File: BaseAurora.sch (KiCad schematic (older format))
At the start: 13 parts

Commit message: esquematico revisado
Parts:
- removed Cin, Cout: 1μF C, symbol Device:C
- removed D?: DIODE, symbol pspice:DIODE
- removed R? (x2): R, symbol Device:R
- removed U?: STM32F030C8Tx, Package_QFP:LQFP-48_7x7mm_P0.5mm, symbol MCU_ST_STM32F0:STM32F030C8Tx
- removed U? (x2): KA78M05_TO252, Package_TO_SOT_SMD:TO-252-2, symbol Regulator_Linear:KA78M05_TO252
- removed Vcc: Battery_Cell, Battery:BatteryHolder_Keystone_2466_1xAAA, symbol Device:Battery_Cell
- added BT?: Battery_Cell, symbol Device:Battery_Cell
- added C? (x2): 10u, symbol Device:C_Small
- added D? (x3): LED_Small, symbol Device:LED_Small
- added D?: D_Small, symbol Device:D_Small
- added F? (x2): Polyfuse_Small, symbol Device:Polyfuse_Small
- added J? (x2): Screw_Terminal_01x02, symbol Connector:Screw_Terminal_01x02
- added J? (x3): Conn_01x04_Male, symbol Connector:Conn_01x04_Male
- added J?: Conn_01x03_Male, symbol Connector:Conn_01x03_Male
- added R? (x10): R_Small, symbol Device:R_Small
- added R?: 1M, symbol Device:R_Small
- added R?: 0, symbol Device:R_Small
- added R?: 100K, symbol Device:R_Small
- added R?: 220K, symbol Device:R_Small
- added U?: E32-915T20D, symbol LoRA:E32-915T20D
- added U?: ME6217C33M5G, symbol BaseAurora:ME6217C33M5G
- added U?: NodeMCU1.0(ESP-12E), symbol MCU_ESP82:NodeMCU1.0(ESP-12E)
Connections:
- net labels added: 3V3, ADC, AcionamentoNiCd, DIO1, DIO2, GND_ISO, InputLora, LedAcionamento, LedAlimentacao, LedErro, M0Lora, M1Lora, OutputLora, SCL_MASTER, SCL_SLAVE, SDA_MASTER, SDA_SLAVE, StatusLora, VCC_ISO, VCC_MCU, VLora, Vbat, Vext
- net labels removed: VCC, Vcc
- wire segments 18 -> 32
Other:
- moved on the sheet: D?

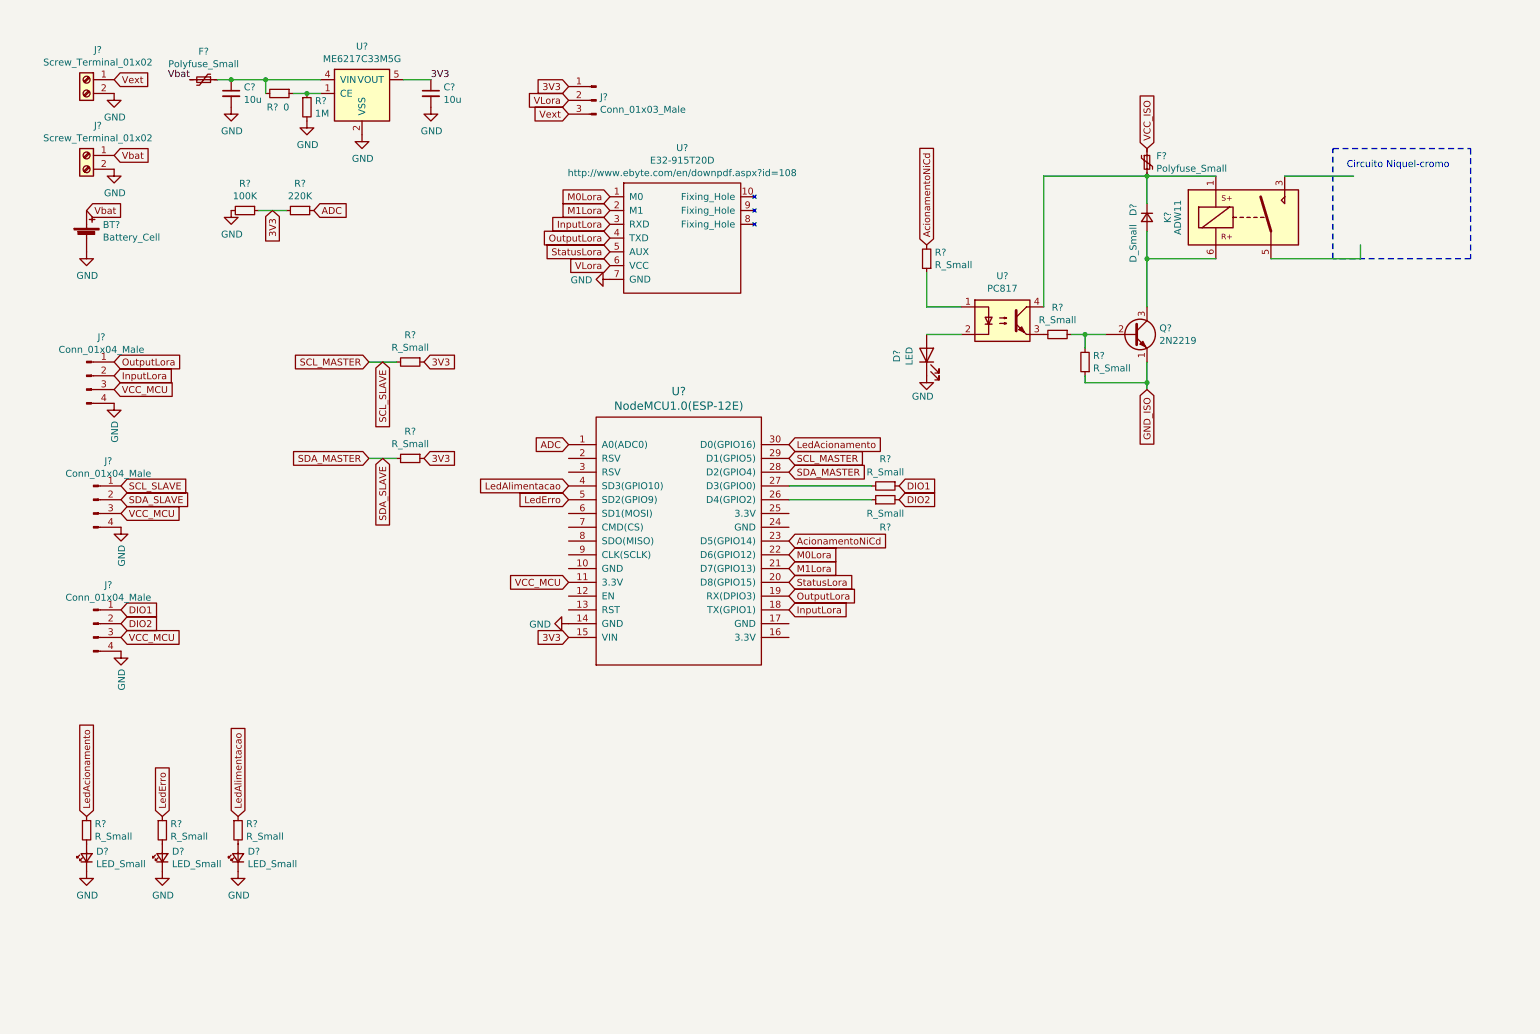
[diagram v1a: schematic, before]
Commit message: Revisão do circuito de acionamento. Atribuição de valores para os componentes. Organização geral do esquemático.
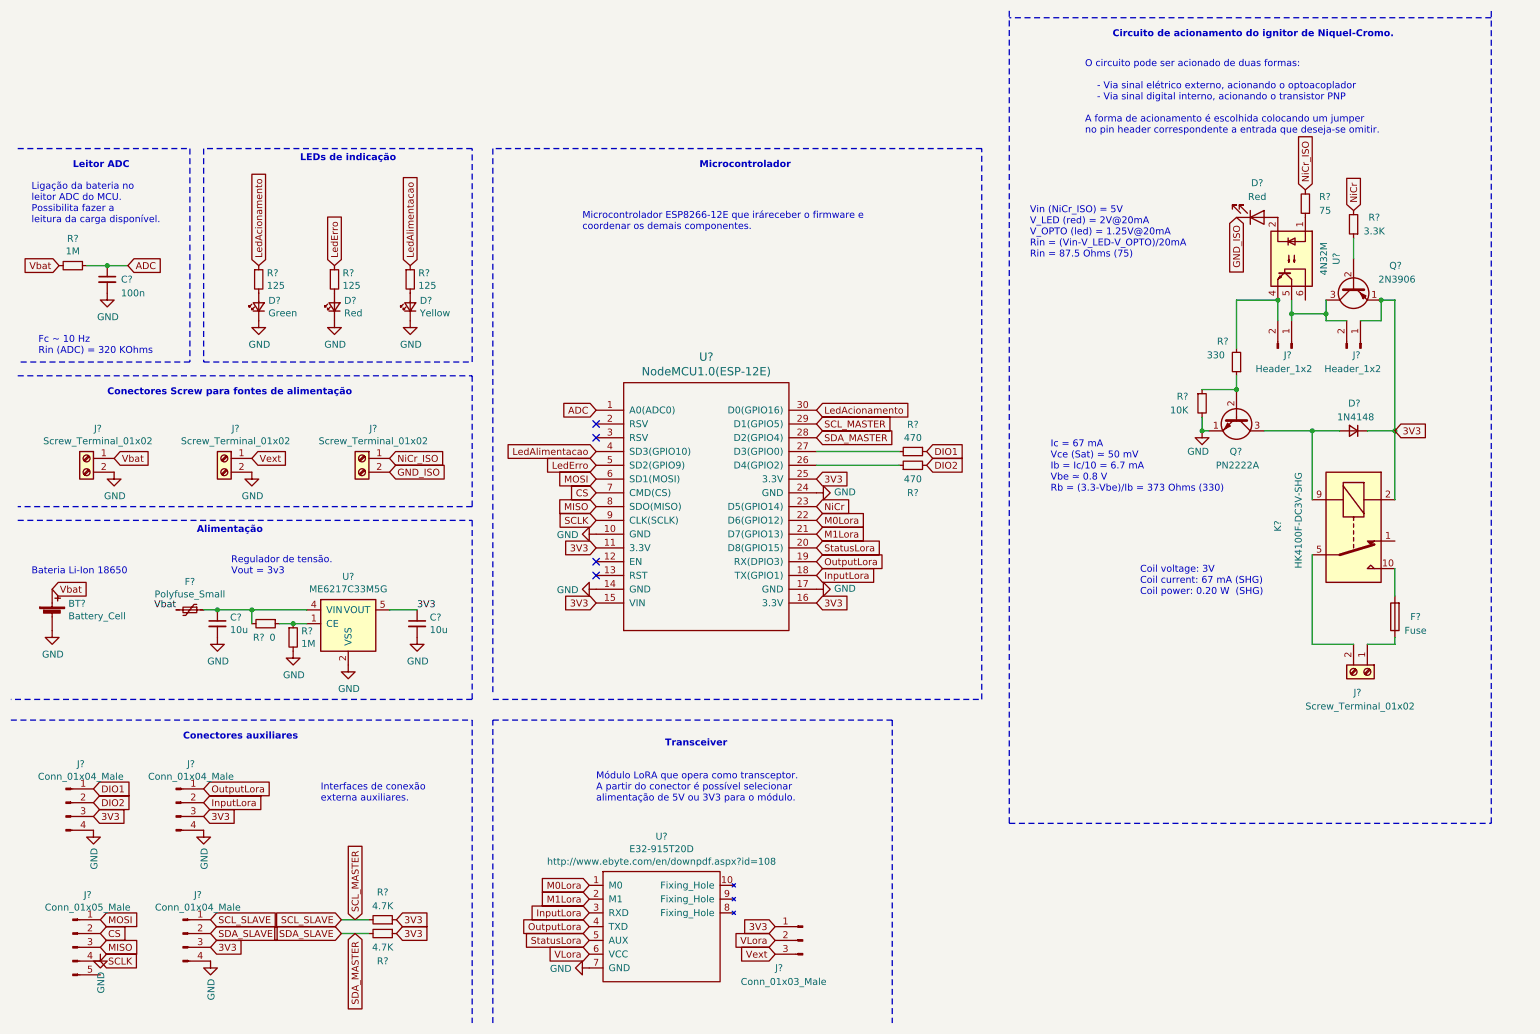
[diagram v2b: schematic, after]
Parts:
- removed F?: Polyfuse_Small, symbol Device:Polyfuse_Small
- removed K?: ADW11, Relay_THT:Relay_1P1T_NO_10x24x18.8mm_Panasonic_ADW11xxxxW_THT, symbol Relay:ADW11
- removed Q?: 2N2219, Package_TO_SOT_THT:TO-39-3, symbol Transistor_BJT:2N2219
- removed R?: 100K, symbol Device:R_Small
- removed U?: PC817, Package_DIP:DIP-4_W7.62mm, symbol Isolator:PC817
- added C?: 100n, symbol Device:C_Small
- added F?: Fuse, symbol Device:Fuse
- added J? (x2): Screw_Terminal_01x02, symbol Connector:Screw_Terminal_01x02
- added J? (x2): Header_1x2, symbol Connector:Conn_01x02_Male
- added J?: Conn_01x05_Male, symbol Connector:Conn_01x05_Male
- added K?: HK4100F-DC3V-SHG, Relay_THT:Relay_SPDT_Omron_G5V-1, symbol Relay:G5V-1
- added Q?: PN2222A, Package_TO_SOT_THT:TO-92_Inline, symbol Transistor_BJT:PN2222A
- added Q?: 2N3906, Package_TO_SOT_THT:TO-92_Inline, symbol Transistor_BJT:2N3906
- added R?: 3.3K, symbol Device:R_Small
- added U?: 4N32M, Package_DIP:DIP-6_W7.62mm, symbol Isolator:4N25
- D?: value LED -> Red
- D?: value LED_Small -> Green
- D?: value LED_Small -> Red
- D?: value LED_Small -> Yellow
- D?: value D_Small -> 1N4148
- R? (x3): value R_Small -> 125
- R? (x2): value R_Small -> 4.7K
- R? (x2): value R_Small -> 470
- R?: value R_Small -> 330
- R?: value R_Small -> 10K
- R?: value R_Small -> 75
- R?: value 220K -> 1M
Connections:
- net labels added: CS, MISO, MOSI, NiCr, NiCr_ISO, SCLK
- net labels removed: AcionamentoNiCd, VCC_ISO, VCC_MCU
- wire segments 32 -> 41
- no-connect marks 0 -> 4
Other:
- note added: "Alimentação\n"
- note added: "Bateria Li-Ion 18650"
- note added: "Circuito de acionamento do ignitor de Niquel-Cromo."
- note added: "Coil voltage: 3V\nCoil current: 67 mA (SHG)\nCoil power: 0.20 W (SHG)"
- note added: "Conectores Screw para fontes de alimentação"
- note added: "Conectores auxiliares"
- note added: "Fc ~~ 10 Hz\nRin (ADC) = 320 KOhms"
- note added: "Ic = 67 mA\nVce (Sat) ≃ 50 mV\nIb = Ic/10 = 6.7 mA\nVbe ≃ 0.8 V\nRb = (3.3-Vbe)/Ib = 373 Ohms (330)"
- note added: "Interfaces de conexão \nexterna auxiliares."
- note added: "LEDs de indicação\n"
- note added: "Leitor ADC"
- note added: "Ligação da bateria no \nleitor ADC do MCU.\nPossibilita fazer a \nleitura da carga disponível."
- note added: "Microcontrolador"
- note added: "Microcontrolador ESP8266-12E que iráreceber o firmware e \ncoordenar os demais componentes."
- note added: "Módulo LoRA que opera como transceptor.\nA partir do conector é possível selecionar\nalimentação de 5V ou 3V3 para o módulo."
- note added: "O circuito pode ser acionado de duas formas:\n\n - Via sinal elétrico externo, acionando o optoacoplador\n - Via sinal digital interno, acionando o transistor PNP\n\nA forma de acionamento é escolhida colocando um jumper \nno pin header correspondente a entrada que deseja-se omitir."
- note added: "Regulador de tensão.\nVout = 3v3\n"
- note added: "Transceiver"
- note added: "Vin (NiCr_ISO) = 5V\nV_LED (red) = 2V@20mA\nV_OPTO (led) = 1.25V@20mA\nRin = (Vin-V_LED-V_OPTO)/20mA \nRin = 87.5 Ohms (75)"
- note removed: "Circuito Niquel-cromo"
- moved on the sheet: BT?, C?, D?, F?, J?, R?, U?

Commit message: Reorganização dos componentes e posicionamento do acionamento do NiCr no pino seguro.
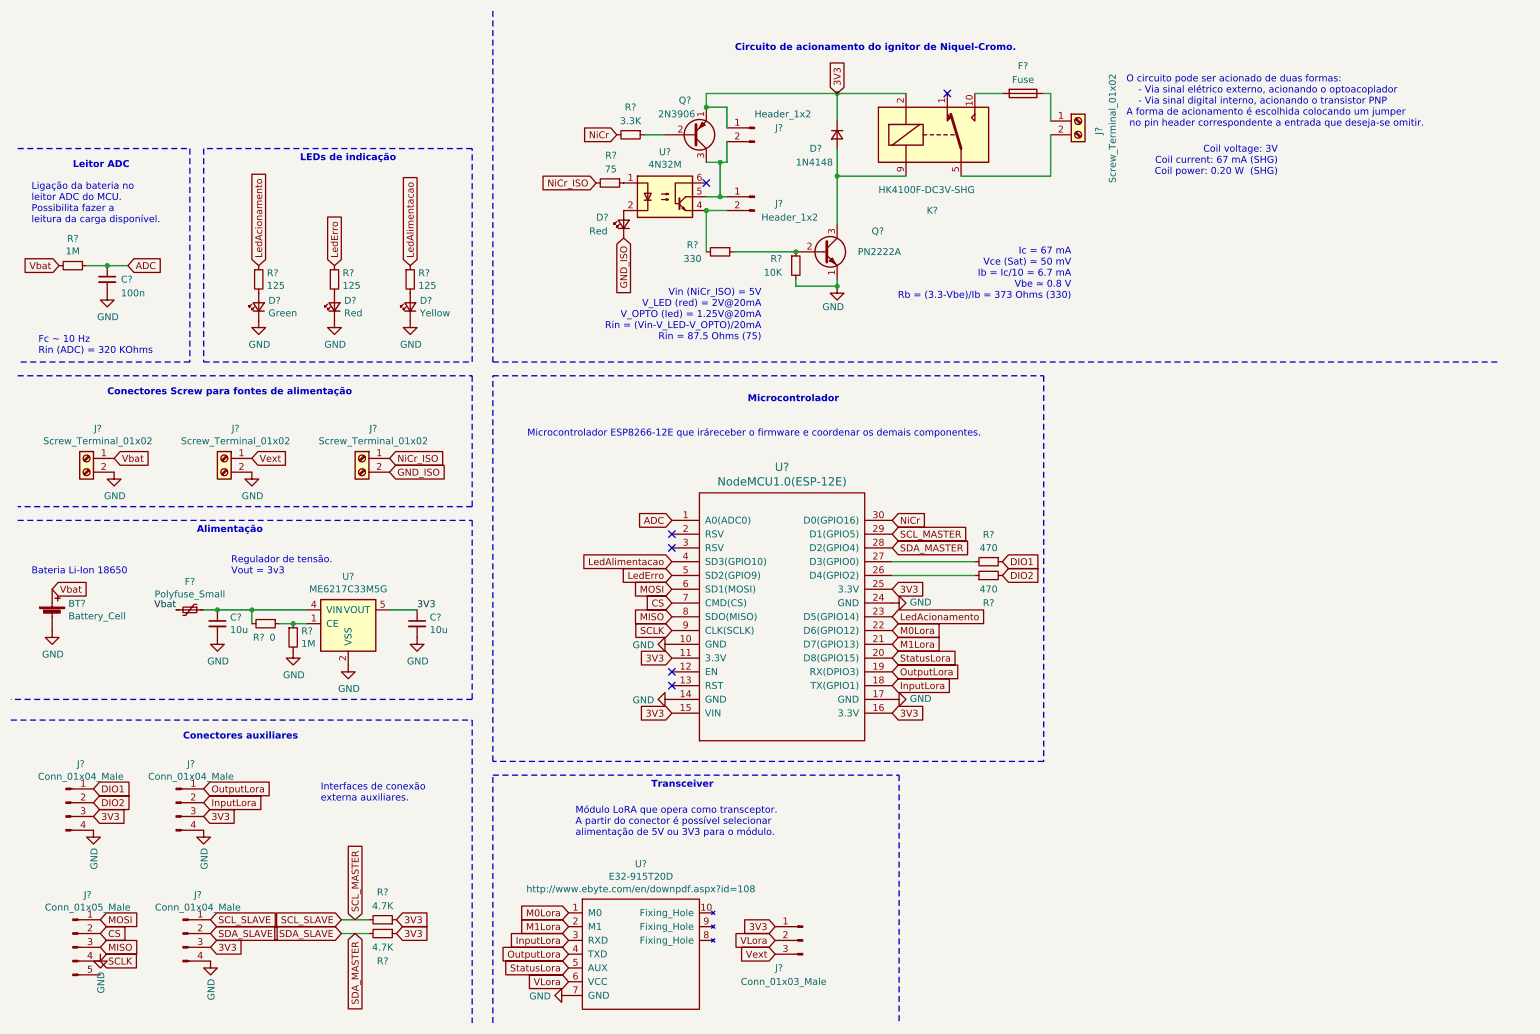
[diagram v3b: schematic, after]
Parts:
- removed D?: Red, symbol Device:LED
- added D?: Red, symbol Device:LED_Small
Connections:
- net GND_ISO: now also D?.1 (K)
- net LedAcionamento: now also U?.23 (D5(GPIO14)); no longer U?.30 (D0(GPIO16))
- net NiCr: now also U?.30 (D0(GPIO16)); no longer U?.23 (D5(GPIO14))
- net at U?.2: now also D?.2 (A)
- no-connect marks 4 -> 6
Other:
- note added: "Microcontrolador ESP8266-12E que iráreceber o firmware e coordenar os demais componentes."
- note added: "O circuito pode ser acionado de duas formas:\n - Via sinal elétrico externo, acionando o optoacoplador\n - Via sinal digital interno, acionando o transistor PNP\nA forma de acionamento é escolhida colocando um jumper\n no pin header correspondente a entrada que deseja-se omitir."
- note removed: "Microcontrolador ESP8266-12E que iráreceber o firmware e \ncoordenar os demais componentes."
- note removed: "O circuito pode ser acionado de duas formas:\n\n - Via sinal elétrico externo, acionando o optoacoplador\n - Via sinal digital interno, acionando o transistor PNP\n\nA forma de acionamento é escolhida colocando um jumper \nno pin header correspondente a entrada que deseja-se omitir."
- moved on the sheet: D?, F?, J?, K?, Q?, R?, U?

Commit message: Design inicial da pcb
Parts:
- BT1: renamed from BT?; footprint (none) -> Battery:BatteryHolder_Keystone_1042_1x18650
- C1, C2, C3: renamed from C?; footprint (none) -> Capacitor_SMD:C_0805_2012Metric
- D1, D2, D3, D4: renamed from D?; footprint (none) -> LED_THT:LED_D3.0mm_Horizontal_O1.27mm_Z2.0mm
- D5: renamed from D?; footprint (none) -> Diode_SMD:D_SOD-123
- F1: renamed from F?; footprint (none) -> Fuse:Fuse_1206_3216Metric_Castellated
- F2: renamed from F?; footprint (none) -> Fuse:Fuseholder_Cylinder-5x20mm_Stelvio-Kontek_PTF78_Horizontal_Open
- J1, J4, J5: renamed from J?; footprint (none) -> Connector_Molex:Molex_KK-254_AE-6410-04A_1x04_P2.54mm_Vertical
- J10: renamed from J?; footprint (none) -> Connector_Molex:Molex_KK-254_AE-6410-03A_1x03_P2.54mm_Vertical
- J11, J3, J6, J7: renamed from J?; footprint (none) -> TerminalBlock_Phoenix:TerminalBlock_Phoenix_MKDS-1,5-2_1x02_P5.00mm_Horizontal
- J2: renamed from J?; footprint (none) -> Connector_Molex:Molex_KK-254_AE-6410-05A_1x05_P2.54mm_Vertical
- J8, J9: renamed from J?; footprint (none) -> Connector_Molex:Molex_KK-254_AE-6410-02A_1x02_P2.54mm_Vertical
- R1, R10, R11, R12, R13, R14, R2, R3, R4, R5, R6, R7, R8, R9: renamed from R?; footprint (none) -> Resistor_SMD:R_0805_2012Metric
- U1: renamed from U?; footprint (none) -> Package_TO_SOT_SMD:SOT-23-5
- U2: renamed from U?; footprint (none) -> LoRA:E32-xxxT20D
- U4: renamed from U?; footprint (none) -> ESP8266:ESP12F-Devkit-V3
- gave numbers to parts that had none: 4
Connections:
- net GND: now also J2.5 (Pin_5), J6.1 (Pin_1); no longer J6.2 (Pin_2)
- net GND_ISO: now also J7.1 (Pin_1); no longer J7.2 (Pin_2)
- net NiCr_ISO: now also J7.2 (Pin_2); no longer J7.1 (Pin_1)
- net Vext: now also J6.2 (Pin_2); no longer J6.1 (Pin_1)
- net at J11.1 (Pin_1): now also K1.5, K1.6; no longer F2.1
- new net: F2.1, J11.2 (Pin_2)
